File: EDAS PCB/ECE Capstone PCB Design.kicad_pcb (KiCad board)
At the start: 2 copper layers, 149.1 x 102.3 mm, 86 parts, among them J1 1053131105, J2 1053131105, J3 Conn_01x40_Socket, U1 MCP2518FDT-H/SL, U2 MCP2542FD-E/SN, U5 TPS562201, U6 TPS61165DBV, U7 TPS562201

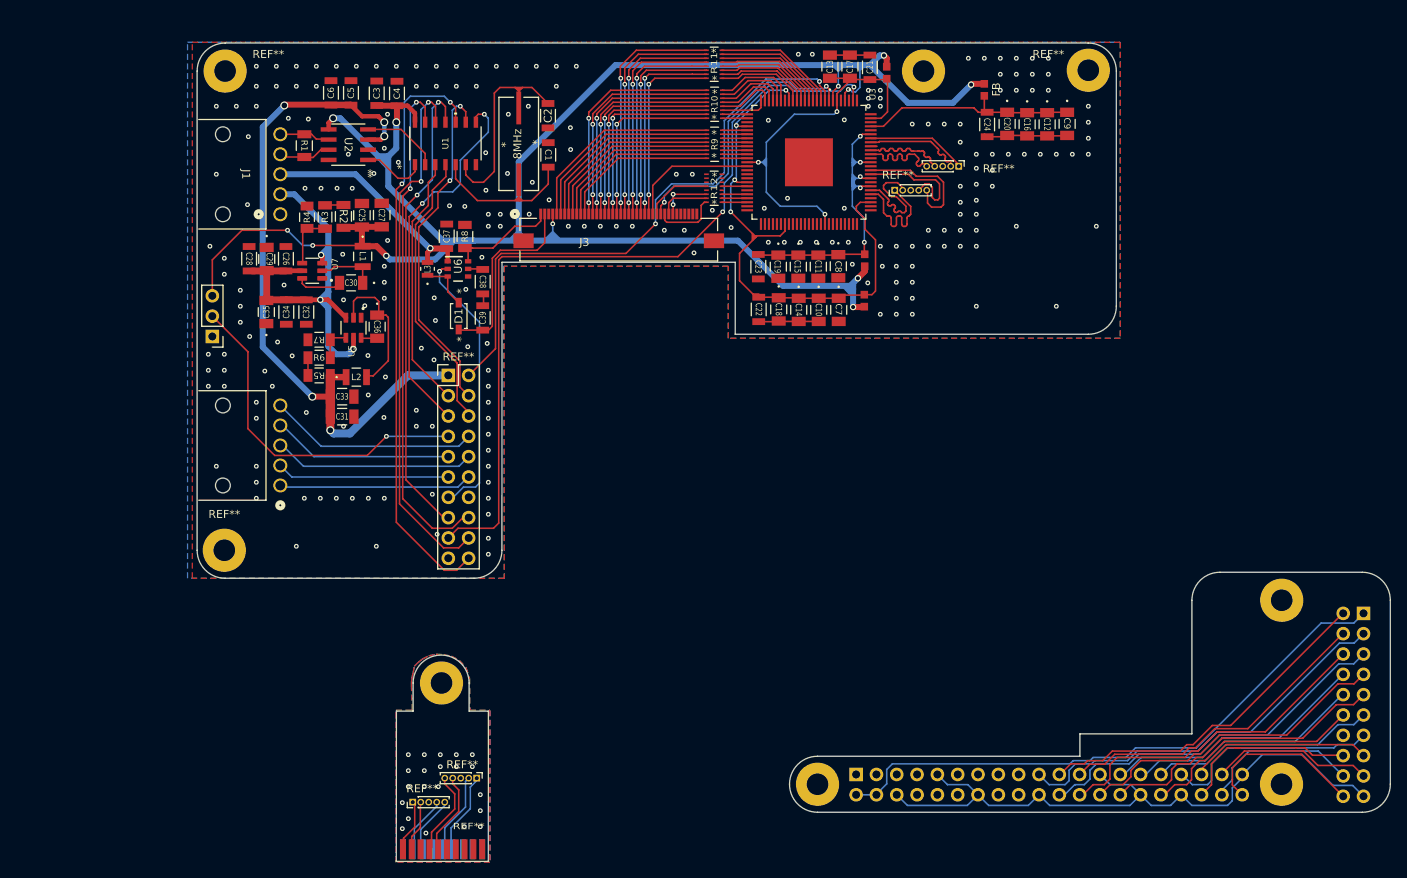
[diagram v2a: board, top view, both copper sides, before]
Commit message: Fixed a whole bunch of issues with the silk screen. Created a new naming convention for the capacitors to reduce the amount of characters in the silk screen. Added thermal relief vias to all of the through hole connections.
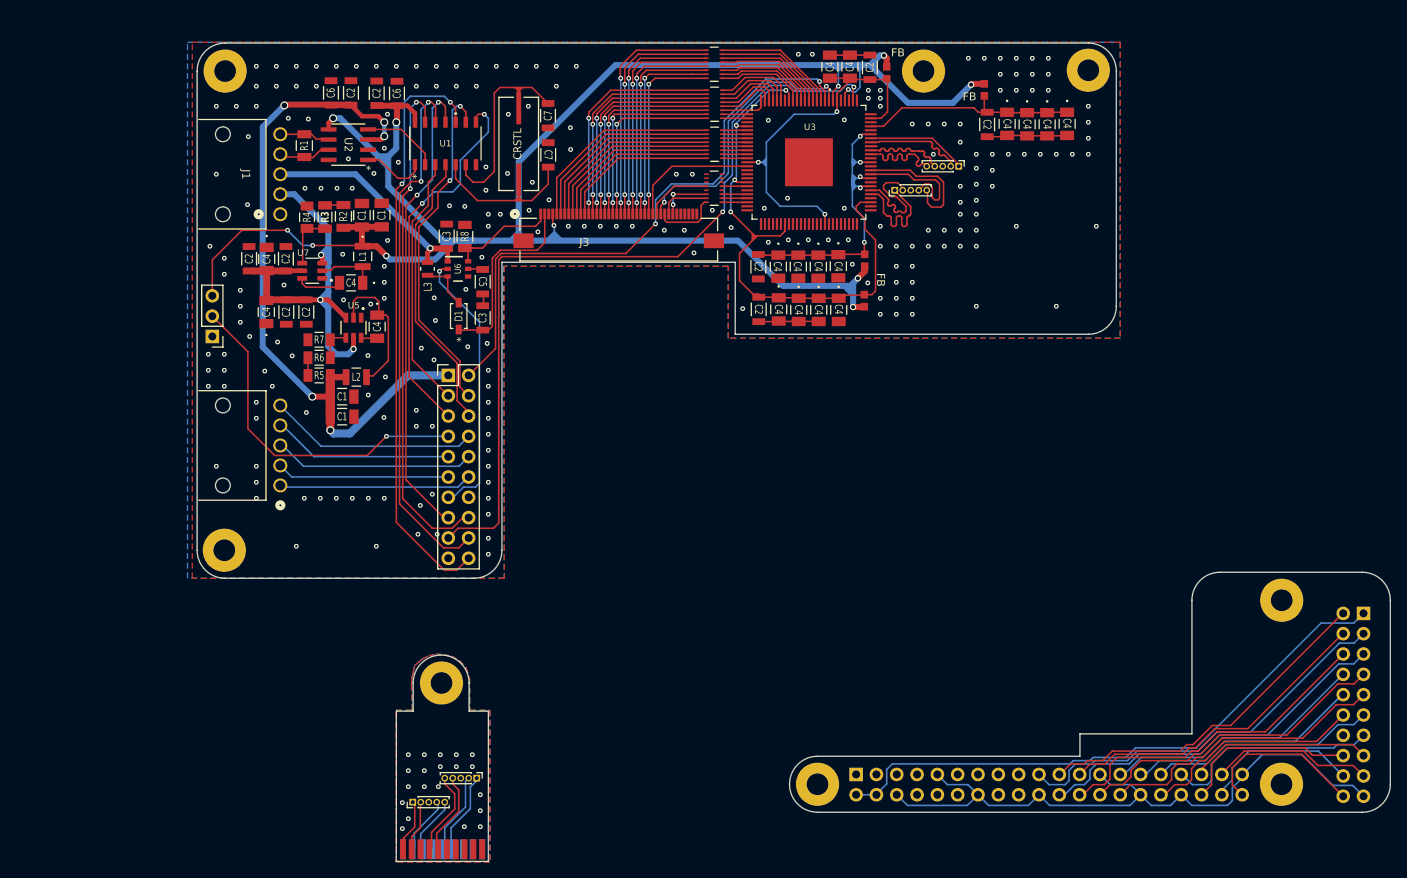
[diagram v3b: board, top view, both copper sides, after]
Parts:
- renumbered C31 to C1, C25 to C1, C27 to C1, C33 to C1, C23 to C2, C34 to C2, C21 to C2, C22 to C2, C28 to C2, C24 to C2, C26 to C2, C5 to C2, C32 to C2, C3 to C2, C37 to C3, C39 to C3, C13 to C4, C14 to C4, C9 to C4, C19 to C4, C7 to C4, C15 to C4, C29 to C4, C30 to C4, C10 to C4, C8 to C4, C12 to C4, C17 to C4, C36 to C4, C16 to C4, C35 to C4, C20 to C4, C18 to C4, C11 to C4, C38 to C5, C4 to C6, C1 to C7, C2 to C7, 8MHz to CRSTL, FB4 to FB, FB2 to FB
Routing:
- net DGND: vias 21 -> 20
- net /GND: vias 226 -> 228
